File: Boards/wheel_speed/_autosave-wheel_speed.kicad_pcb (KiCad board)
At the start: 2 copper layers, 38.1 x 50.8 mm, 42 parts, among them J1 CONN_02X03, J2 MM_F_RA_08, U1 MCP2561-E_SN, U101 TPS560430YF, U2 ATMEGA16M1, Y1 Crystal_SMD

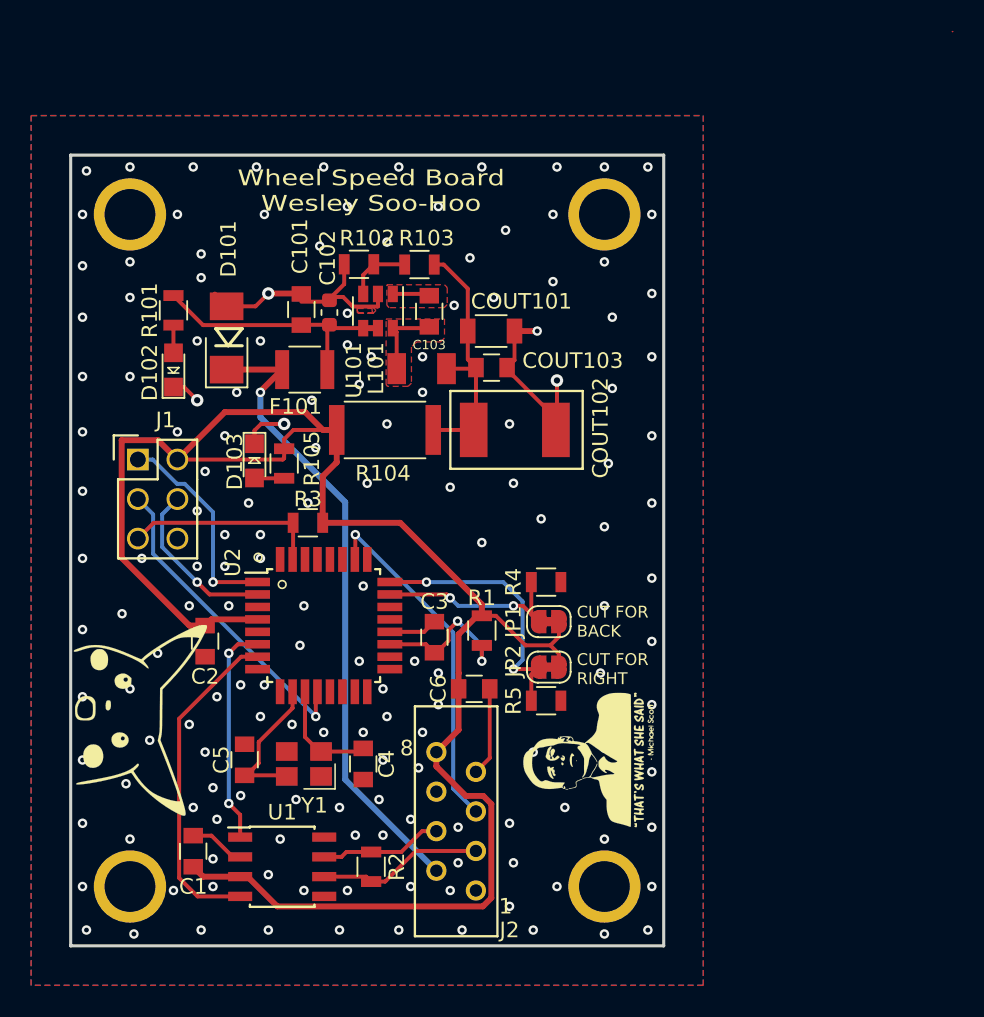
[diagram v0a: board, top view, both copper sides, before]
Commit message: update readme to reflect new pinout
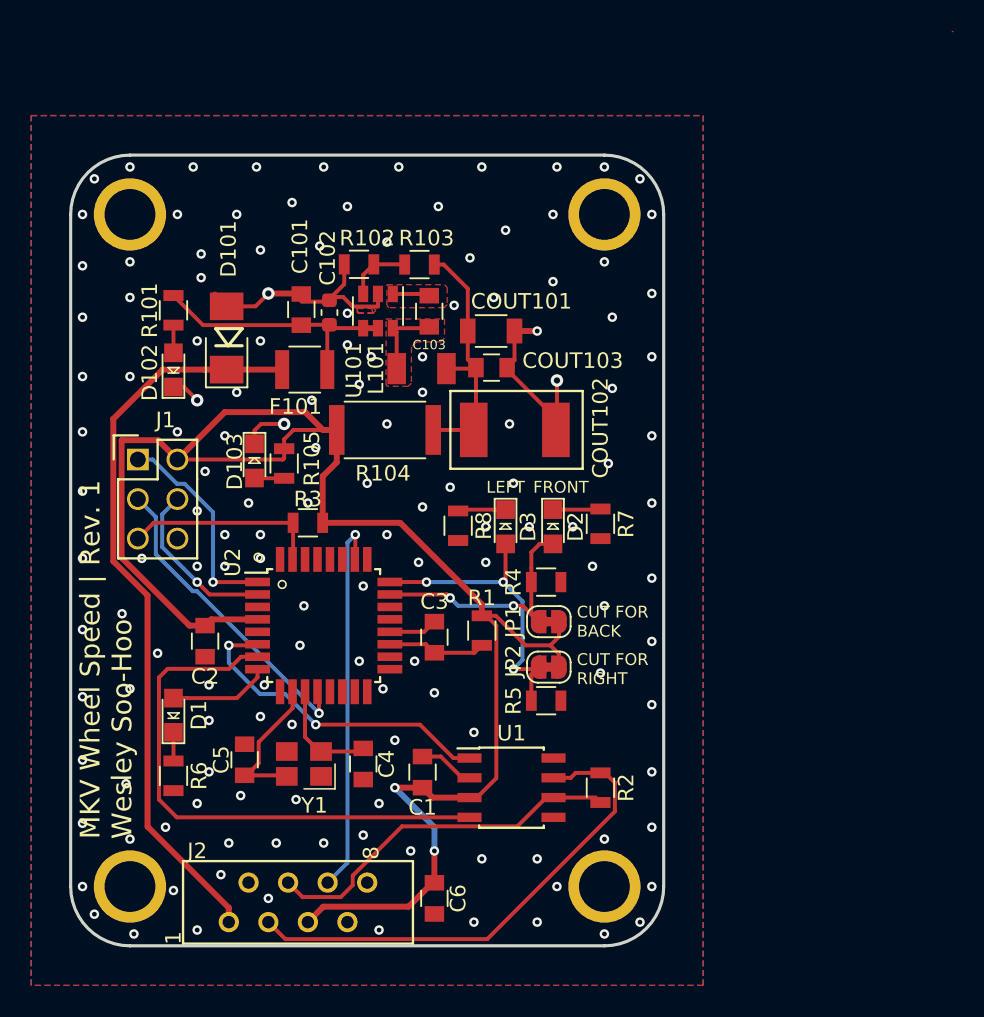
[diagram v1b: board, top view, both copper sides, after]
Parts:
- removed the G*** at (105.4, 112.3)
- removed the G*** at (134.9, 115.1)
- added D1: LED_0805, footprints:LED_0805_OEM, F.Cu at (108.2, 112.2)
- added D2: LED_0805, footprints:LED_0805_OEM, F.Cu at (132.6, 100.1)
- added D3: LED_0805, footprints:LED_0805_OEM, F.Cu at (129.5, 100.1)
- added R6: R_120, footprints:R_0805_OEM, F.Cu at (108.2, 116.1)
- added R7: R_120, footprints:R_0805_OEM, F.Cu at (135.6, 99.9)
- added R8: R_120, footprints:R_0805_OEM, F.Cu at (126.5, 100.0)
- moved C1 15.6 mm to (124.2, 115.8)
- moved R2 15.6 mm to (135.6, 116.8)
- moved U1 15.6 mm to (129.9, 116.8)
- moved C6 13.7 mm to (125.0, 124.0), turned to 90 degrees
- moved J2 12.9 mm to (116.8, 125.5), turned to 90 degrees
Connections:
- C6 pad 1: VCC -> GND
- C6 pad 2: GND -> VCC
- J2 pad 1: GND -> /12V
- J2 pad 2: /12V -> GND
- J2 pad 3: /CAN_LO -> /CAN_HI
- J2 pad 4: /CAN_HI -> /CAN_LO
- J2 pad 5: /SENSE_IN -> VCC
- J2 pad 6: GND -> /SENSE_IN
- J2 pad 8: VCC -> GND
- U2 pad 8: Net-(U2-Pad8) -> /DEBUG
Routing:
- net /CAN_HI: track 7.89 -> 32.3 mm
- net /CAN_RX: track 21.3 -> 35.1 mm
- net /CAN_LO: track 10.7 -> 23.6 mm
- net VCC: track 116.5 -> 109.1 mm, vias 0 -> 2
- net /CAN_TX: track 14.2 -> 21.0 mm
- net /12V: track 41.3 -> 47.9 mm, vias 1 -> 0
- net /DEBUG: track 0.00 -> 6.48 mm
- net GND: track 44.8 -> 39.1 mm, vias 160 -> 144
- net Net-(C3-Pad1): track 10.0 -> 6.33 mm, vias 2 -> 0
- net /FRONT_SENSE: track 13.0 -> 16.6 mm
- net Net-(D3-Pad1): track 0.00 -> 3.08 mm
- net Net-(D2-Pad1): track 0.00 -> 3.06 mm
- net /LEFT_SENSE: track 17.7 -> 20.2 mm, vias 2 -> 3
- net /SENSE_IN: track 22.6 -> 24.7 mm
- net Net-(D1-Pad1): track 0.00 -> 1.84 mm
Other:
- outline, holes or cut-outs redrawn
- board text added: "FRONT"
- board text added: "LEFT"
- board text added: "MKV Wheel Speed | Rev. 1 Wesley Soo-Hoo"
- board text removed: "Wheel Speed Board Wesley Soo-Hoo"
